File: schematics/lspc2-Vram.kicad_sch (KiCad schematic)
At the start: 2 parts

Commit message: update readme
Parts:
- renumbered 4B to 4B1, 5B to 5B1
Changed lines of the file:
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@@
     (effects (font (size 1.27 1.27)) (justify left bottom))
   )
-  (label "F15" (at 86.36 132.08 0)
-    (effects (font (size 1.27 1.27)) (justify left bottom))
-  )
-  (label "F14" (at 86.36 129.54 0)
-    (effects (font (size 1.27 1.27)) (justify left bottom))
-  )
-  (label "F12" (at 86.36 124.46 0)
-    (effects (font (size 1.27 1.27)) (justify left bottom))
-  )
-  (label "B13" (at 43.18 99.06 0)
+  (label "F15" (at 86.36 132.08 0) (fields_autoplaced)
+    (effects (font (size 1.27 1.27)) (justify left bottom))
+  )
+  (label "F14" (at 86.36 129.54 0) (fields_autoplaced)
+    (effects (font (size 1.27 1.27)) (justify left bottom))
+  )
+  (label "F12" (at 86.36 124.46 0) (fields_autoplaced)
+    (effects (font (size 1.27 1.27)) (justify left bottom))
+  )
+  (label "B13" (at 43.18 99.06 0) (fields_autoplaced)
     (effects (font (size 1.27 1.27)) (justify left bottom))
   )
@@
     (effects (font (size 1.27 1.27)) (justify left bottom))
   )
-  (label "F0" (at 86.36 66.04 0)
+  (label "F0" (at 86.36 66.04 0) (fields_autoplaced)
     (effects (font (size 1.27 1.27)) (justify left bottom))
   )
@@
     (effects (font (size 1.27 1.27)) (justify left bottom))
   )
-  (label "F13" (at 86.36 127 0)
-    (effects (font (size 1.27 1.27)) (justify left bottom))
-  )
-  (label "F6" (at 86.36 81.28 0)
-    (effects (font (size 1.27 1.27)) (justify left bottom))
-  )
-  (label "B12" (at 43.18 96.52 0)
-    (effects (font (size 1.27 1.27)) (justify left bottom))
-  )
-  (label "B11" (at 43.18 93.98 0)
-    (effects (font (size 1.27 1.27)) (justify left bottom))
-  )
-  (label "F4" (at 86.36 76.2 0)
-    (effects (font (size 1.27 1.27)) (justify left bottom))
-  )
-  (label "F11" (at 86.36 121.92 0)
-    (effects (font (size 1.27 1.27)) (justify left bottom))
-  )
-  (label "B0" (at 43.18 66.04 0)
+  (label "F13" (at 86.36 127 0) (fields_autoplaced)
+    (effects (font (size 1.27 1.27)) (justify left bottom))
+  )
+  (label "F6" (at 86.36 81.28 0) (fields_autoplaced)
+    (effects (font (size 1.27 1.27)) (justify left bottom))
+  )
+  (label "B12" (at 43.18 96.52 0) (fields_autoplaced)
+    (effects (font (size 1.27 1.27)) (justify left bottom))
+  )
+  (label "B11" (at 43.18 93.98 0) (fields_autoplaced)
+    (effects (font (size 1.27 1.27)) (justify left bottom))
+  )
+  (label "F4" (at 86.36 76.2 0) (fields_autoplaced)
+    (effects (font (size 1.27 1.27)) (justify left bottom))
+  )
+  (label "F11" (at 86.36 121.92 0) (fields_autoplaced)
+    (effects (font (size 1.27 1.27)) (justify left bottom))
+  )
+  (label "B0" (at 43.18 66.04 0) (fields_autoplaced)
     (effects (font (size 1.27 1.27)) (justify left bottom))
   )
@@
     (effects (font (size 1.27 1.27)) (justify left bottom))
   )
-  (label "B3" (at 43.18 73.66 0)
+  (label "B3" (at 43.18 73.66 0) (fields_autoplaced)
     (effects (font (size 1.27 1.27)) (justify left bottom))
   )
@@
     (effects (font (size 1.27 1.27)) (justify left bottom))
   )
-  (label "F8" (at 86.36 114.3 0)
-    (effects (font (size 1.27 1.27)) (justify left bottom))
-  )
-  (label "F1" (at 86.36 68.58 0)
-    (effects (font (size 1.27 1.27)) (justify left bottom))
-  )
-  (label "B10" (at 43.18 91.44 0)
-    (effects (font (size 1.27 1.27)) (justify left bottom))
-  )
-  (label "B4" (at 43.18 76.2 0)
+  (label "F8" (at 86.36 114.3 0) (fields_autoplaced)
+    (effects (font (size 1.27 1.27)) (justify left bottom))
+  )
+  (label "F1" (at 86.36 68.58 0) (fields_autoplaced)
+    (effects (font (size 1.27 1.27)) (justify left bottom))
+  )
+  (label "B10" (at 43.18 91.44 0) (fields_autoplaced)
+    (effects (font (size 1.27 1.27)) (justify left bottom))
+  )
+  (label "B4" (at 43.18 76.2 0) (fields_autoplaced)
     (effects (font (size 1.27 1.27)) (justify left bottom))
   )
@@
     (effects (font (size 1.27 1.27)) (justify left bottom))
   )
-  (label "B7" (at 43.18 83.82 0)
-    (effects (font (size 1.27 1.27)) (justify left bottom))
-  )
-  (label "B5" (at 43.18 78.74 0)
-    (effects (font (size 1.27 1.27)) (justify left bottom))
-  )
-  (label "B8" (at 43.18 86.36 0)
-    (effects (font (size 1.27 1.27)) (justify left bottom))
-  )
-  (label "F2" (at 86.36 71.12 0)
-    (effects (font (size 1.27 1.27)) (justify left bottom))
-  )
-  (label "B2" (at 43.18 71.12 0)
-    (effects (font (size 1.27 1.27)) (justify left bottom))
-  )
-  (label "F10" (at 86.36 119.38 0)
-    (effects (font (size 1.27 1.27)) (justify left bottom))
-  )
-  (label "F7" (at 86.36 83.82 0)
+  (label "B7" (at 43.18 83.82 0) (fields_autoplaced)
+    (effects (font (size 1.27 1.27)) (justify left bottom))
+  )
+  (label "B5" (at 43.18 78.74 0) (fields_autoplaced)
+    (effects (font (size 1.27 1.27)) (justify left bottom))
+  )
+  (label "B8" (at 43.18 86.36 0) (fields_autoplaced)
+    (effects (font (size 1.27 1.27)) (justify left bottom))
+  )
+  (label "F2" (at 86.36 71.12 0) (fields_autoplaced)
+    (effects (font (size 1.27 1.27)) (justify left bottom))
+  )
+  (label "B2" (at 43.18 71.12 0) (fields_autoplaced)
+    (effects (font (size 1.27 1.27)) (justify left bottom))
+  )
+  (label "F10" (at 86.36 119.38 0) (fields_autoplaced)
+    (effects (font (size 1.27 1.27)) (justify left bottom))
+  )
+  (label "F7" (at 86.36 83.82 0) (fields_autoplaced)
     (effects (font (size 1.27 1.27)) (justify left bottom))
   )
@@
     (effects (font (size 1.27 1.27)) (justify left bottom))
   )
-  (label "F9" (at 86.36 116.84 0)
-    (effects (font (size 1.27 1.27)) (justify left bottom))
-  )
-  (label "B9" (at 43.18 88.9 0)
+  (label "F9" (at 86.36 116.84 0) (fields_autoplaced)
+    (effects (font (size 1.27 1.27)) (justify left bottom))
+  )
+  (label "B9" (at 43.18 88.9 0) (fields_autoplaced)
     (effects (font (size 1.27 1.27)) (justify left bottom))
   )
@@
     (effects (font (size 1.27 1.27)) (justify left bottom))
   )
-  (label "F5" (at 86.36 78.74 0)
+  (label "F5" (at 86.36 78.74 0) (fields_autoplaced)
     (effects (font (size 1.27 1.27)) (justify left bottom))
   )
@@
     (effects (font (size 1.27 1.27)) (justify left bottom))
   )
-  (label "F3" (at 86.36 73.66 0)
+  (label "F3" (at 86.36 73.66 0) (fields_autoplaced)
     (effects (font (size 1.27 1.27)) (justify left bottom))
   )
@@
     (effects (font (size 1.27 1.27)) (justify left bottom))
   )
-  (label "B1" (at 43.18 68.58 0)
-    (effects (font (size 1.27 1.27)) (justify left bottom))
-  )
-  (label "B14" (at 43.18 101.6 0)
-    (effects (font (size 1.27 1.27)) (justify left bottom))
-  )
-  (label "B6" (at 43.18 81.28 0)
+  (label "B1" (at 43.18 68.58 0) (fields_autoplaced)
+    (effects (font (size 1.27 1.27)) (justify left bottom))
+  )
+  (label "B14" (at 43.18 101.6 0) (fields_autoplaced)
+    (effects (font (size 1.27 1.27)) (justify left bottom))
+  )
+  (label "B6" (at 43.18 81.28 0) (fields_autoplaced)
     (effects (font (size 1.27 1.27)) (justify left bottom))
   )
@@
   (symbol (lib_id "Memory_RAM:KM62256CLP") (at 64.77 83.82 0) (unit 1)
     (in_bom yes) (on_board yes) (dnp no)
-    (property "Reference" "4B" (at 54.61 62.23 0)
+    (property "Reference" "4B1" (at 54.61 62.23 0)
       (effects (font (size 1.27 1.27)) (justify left))
     )
@@
       (project "MVS"
         (path "/8d0803ab-15ed-47a7-8dcb-ab27dc5b29c2/5f943e9e-0280-4d4f-b6a1-cb23eca420c0"
-          (reference "4B") (unit 1)
+          (reference "4B1") (unit 1)
         )
       )
@@
   (symbol (lib_id "Memory_RAM:KM62256CLP") (at 64.77 132.08 0) (unit 1)
     (in_bom yes) (on_board yes) (dnp no)
-    (property "Reference" "5B" (at 54.61 110.49 0)
+    (property "Reference" "5B1" (at 54.61 110.49 0)
       (effects (font (size 1.27 1.27)) (justify left))
     )
@@
       (project "MVS"
         (path "/8d0803ab-15ed-47a7-8dcb-ab27dc5b29c2/5f943e9e-0280-4d4f-b6a1-cb23eca420c0"
-          (reference "5B") (unit 1)
+          (reference "5B1") (unit 1)
         )
       )

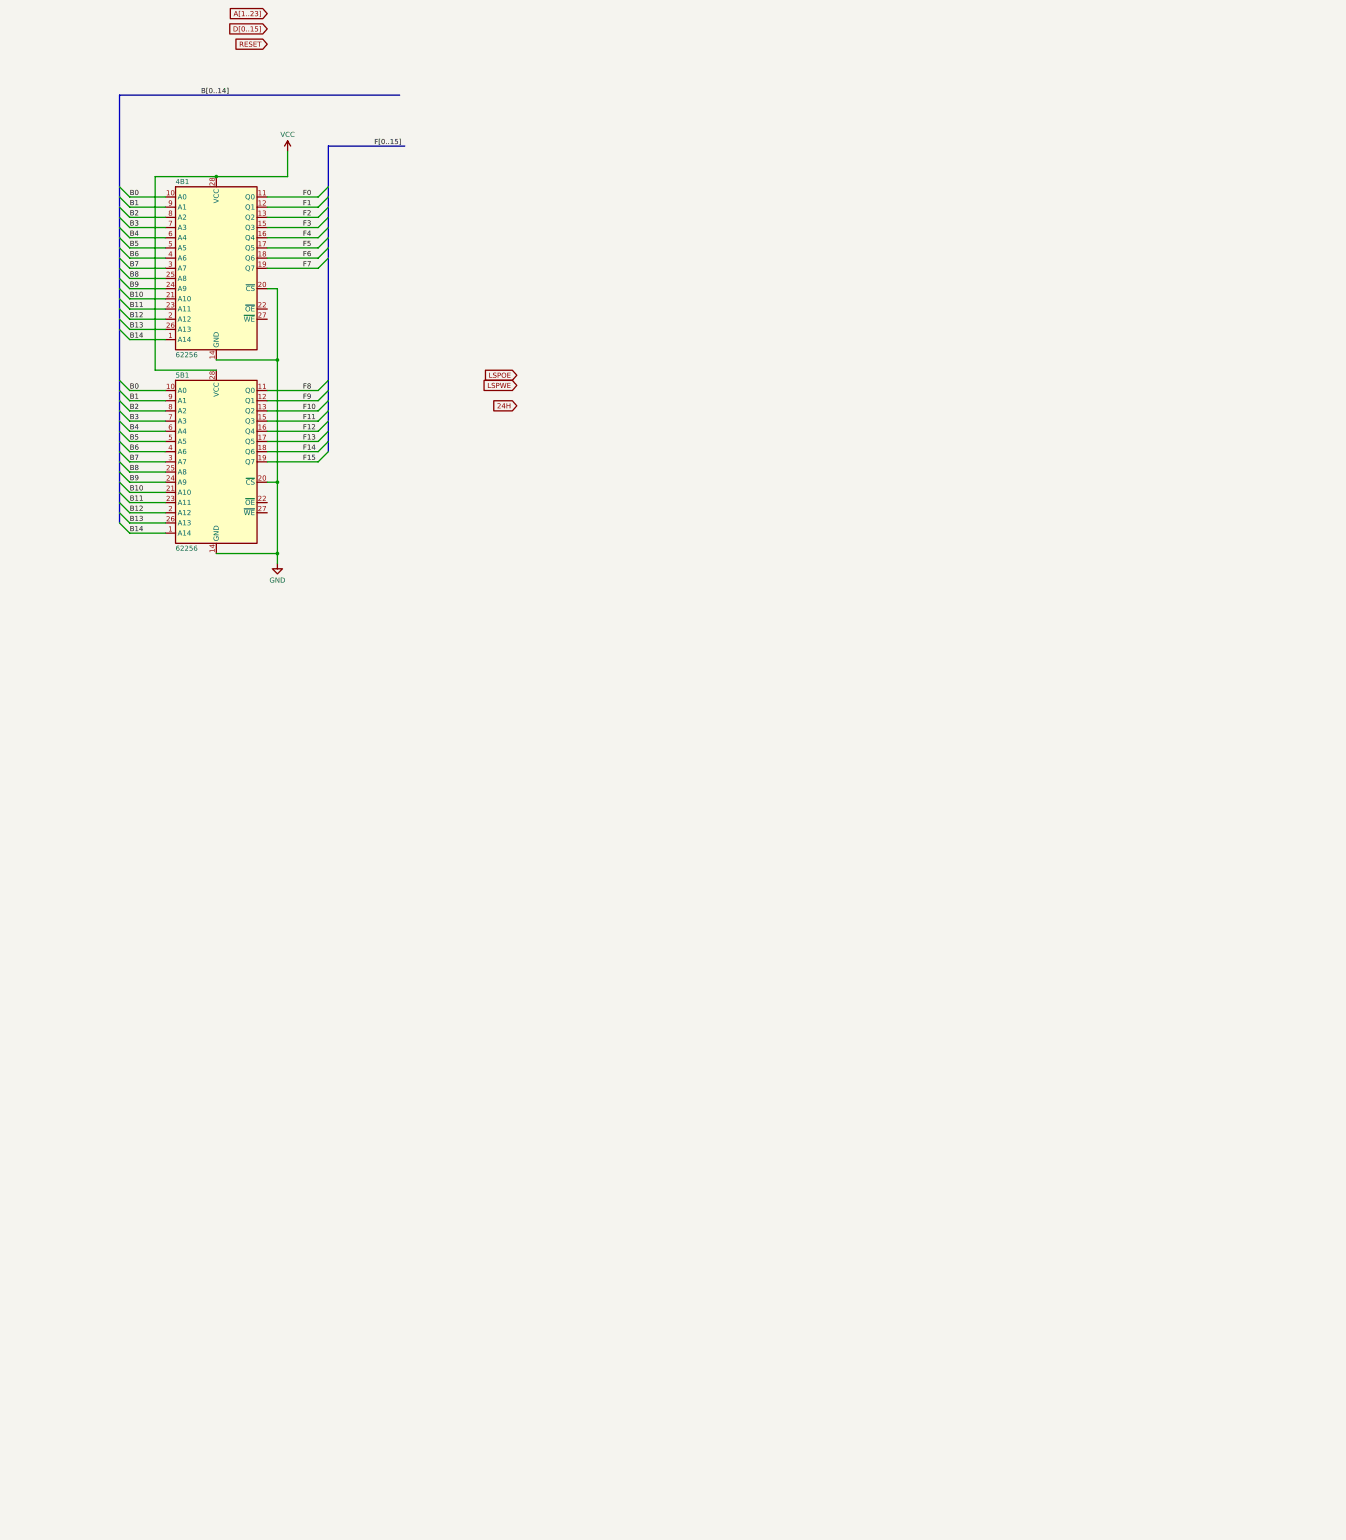
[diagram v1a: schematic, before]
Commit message: update "main" schematics
Adding LSPC2-A2, NEO-B1, L0 ROM
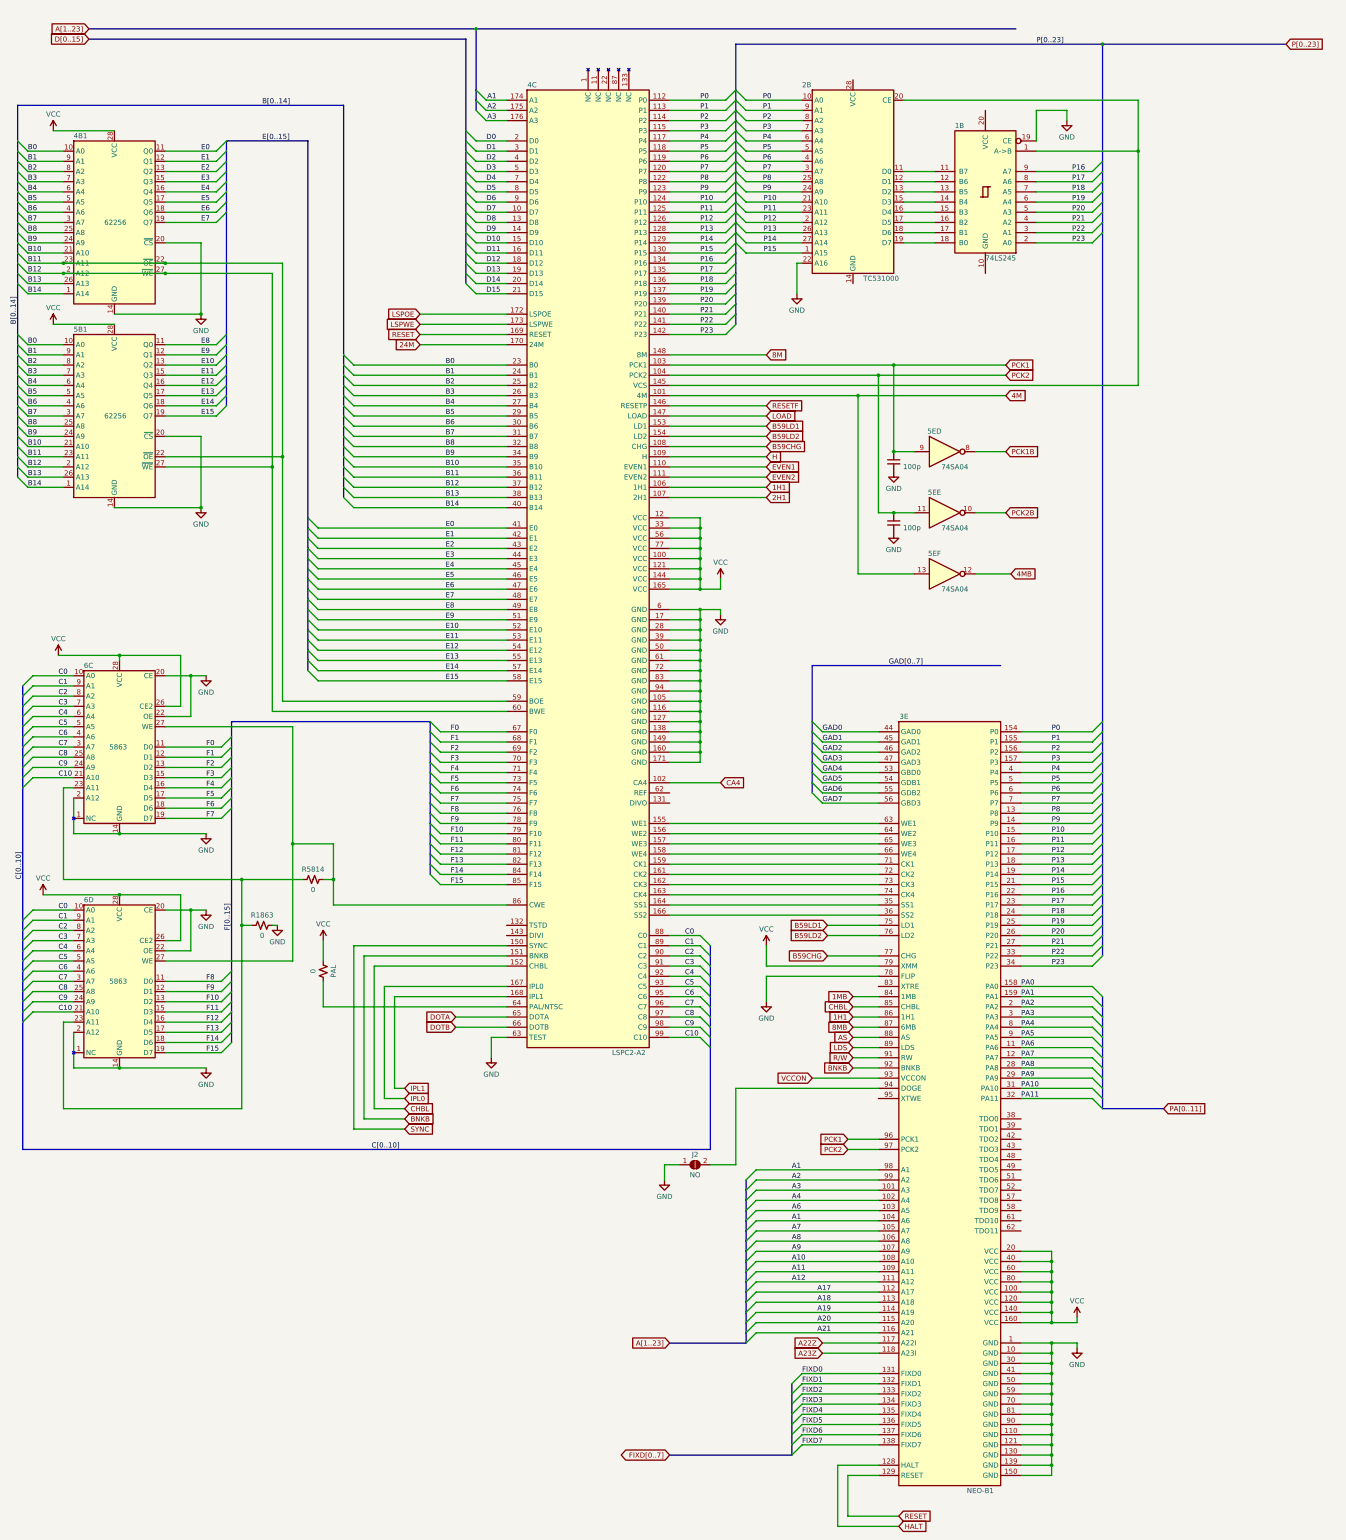
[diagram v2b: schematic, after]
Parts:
- added 1B: 74LS245, symbol 74xx:74LS245
- added 2B: TC531000, Package_DIP:DIP-28_W15.24mm, symbol 0-Custom-SNK:TC531000AP
- added 3E: NEO-B1, symbol 0-Custom-SNK:NEO-B1
- added 4C: LSPC2-A2, symbol 0-Custom-SNK:LSPC2-A2
- added 5E: 74SA04, symbol 74xx:74HC04
- added 6C, 6D: 5863, Package_DIP:DIP-28_W7.62mm, symbol 0-Custom-SNK:CXK5863AP
- added C4, C5: 100p, symbol Device:C_Small
- added J2: NO, symbol Jumper:SolderJumper_2_Open
- added PAL, R1863, R5814: 0, symbol Device:R_Small_US
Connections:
- net B0: now also 4C.23 (B0)
- net B1: now also 4C.24 (B1)
- net B10: now also 4C.35 (B10)
- net B11: now also 4B1.22 (~{OE}), 5B1.22 (~{OE}), 4C.36 (B11), 4C.59 (BOE)
- net B12: now also 4B1.27 (~{WE}), 5B1.27 (~{WE}), 4C.37 (B12), 4C.60 (BWE)
- net B13: now also 4C.38 (B13)
- net B14: now also 4C.40 (B14)
- net B2: now also 4C.25 (B2)
- net B3: now also 4C.26 (B3)
- net B4: now also 4C.27 (B4)
- net B5: now also 4C.29 (B5)
- net B6: now also 4C.30 (B6)
- net B7: now also 4C.31 (B7)
- net B8: now also 4C.32 (B8)
- net B9: now also 4C.34 (B9)
- net F0: now also 4C.67 (F0), 6C.11 (D0); no longer 4B1.11 (Q0)
- net F1: now also 4C.68 (F1), 6C.12 (D1); no longer 4B1.12 (Q1)
- net F10: now also 4C.79 (F10), 6D.13 (D2); no longer 5B1.13 (Q2)
- net F11: now also 4C.80 (F11), 6D.15 (D3); no longer 5B1.15 (Q3)
- net F12: now also 4C.81 (F12), 6D.16 (D4); no longer 5B1.16 (Q4)
- net F13: now also 4C.82 (F13), 6D.17 (D5); no longer 5B1.17 (Q5)
- net F14: now also 4C.84 (F14), 6D.18 (D6); no longer 5B1.18 (Q6)
- net F15: now also 4C.85 (F15), 6D.19 (D7); no longer 5B1.19 (Q7)
- net F2: now also 4C.69 (F2), 6C.13 (D2); no longer 4B1.13 (Q2)
- net F3: now also 4C.70 (F3), 6C.15 (D3); no longer 4B1.15 (Q3)
- net F4: now also 4C.71 (F4), 6C.16 (D4); no longer 4B1.16 (Q4)
- net F5: now also 4C.73 (F5), 6C.17 (D5); no longer 4B1.17 (Q5)
- net F6: now also 4C.74 (F6), 6C.18 (D6); no longer 4B1.18 (Q6)
- net F7: now also 4C.75 (F7), 6C.19 (D7); no longer 4B1.19 (Q7)
- net F8: now also 4C.76 (F8), 6D.11 (D0); no longer 5B1.11 (Q0)
- net F9: now also 4C.78 (F9), 6D.12 (D1); no longer 5B1.12 (Q1)
- net GND: now also 1B.19 (CE), 2B.22 (A16), 3E.1 (GND), 3E.10 (GND), 3E.110 (GND), 3E.121 (GND), 3E.130 (GND), 3E.139 (GND), 3E.150 (GND), 3E.30 (GND), 3E.41 (GND), 3E.50 (GND), 3E.59 (GND), 3E.70 (GND), 3E.78 (FLIP), 3E.81 (GND), 3E.90 (GND), 4C.105 (GND), 4C.116 (GND), 4C.127 (GND), 4C.138 (GND), 4C.149 (GND), 4C.160 (GND), 4C.17 (GND), 4C.171 (GND), 4C.28 (GND), 4C.39 (GND), 4C.50 (GND), 4C.6 (GND), 4C.61 (GND), 4C.63 (TEST), 4C.72 (GND), 4C.83 (GND), 4C.94 (GND), 6C.14 (GND), 6C.2 (A12), 6C.20 (CE), 6C.22 (OE), 6D.14 (GND), 6D.2 (A12), 6D.20 (CE), 6D.22 (OE), C4.2, C5.2, J2.1 (A), R1863.2
- net LSPOE: now also 4C.172 (LSPOE)
- net LSPWE: now also 4C.173 (LSPWE)
- net RESET: now also 3E.129 (RESET), 4C.169 (RESET)
- net VCC: now also 3E.100 (VCC), 3E.120 (VCC), 3E.140 (VCC), 3E.160 (VCC), 3E.20 (VCC), 3E.40 (VCC), 3E.60 (VCC), 3E.79 (XMM), 3E.80 (VCC), 4C.100 (VCC), 4C.12 (VCC), 4C.121 (VCC), 4C.144 (VCC), 4C.165 (VCC), 4C.33 (VCC), 4C.56 (VCC), 4C.77 (VCC), 6C.26 (CE2), 6C.28 (VCC), 6D.26 (CE2), 6D.28 (VCC), PAL.1
- new net: 6C.23 (A11), 6D.23 (A11), R1863.1, R5814.1
- new net: 4C.86 (CWE), 6C.27 (WE), 6D.27 (WE), R5814.2
- new net: 1B.11 (B7), 2B.11 (D0)
- new net: 1B.12 (B6), 2B.12 (D1)
- new net: 1B.13 (B5), 2B.13 (D2)
- new net: 1B.14 (B4), 2B.15 (D3)
- new net: 1B.15 (B3), 2B.16 (D4)
- new net: 1B.16 (B2), 2B.17 (D5)
- new net: 1B.17 (B1), 2B.18 (D6)
- new net: 1B.18 (B0), 2B.19 (D7)
- new net: 1B.1 (A->B), 2B.20 (CE), 4C.145 (VCS)
- new net: 3E.94 (DOGE), J2.2 (B)
- new net: 4C.64 (PAL/NTSC), PAL.2
- new net: 3E.63 (WE1), 4C.155 (WE1)
- new net: 3E.64 (WE2), 4C.156 (WE2)
- new net: 3E.65 (WE3), 4C.157 (WE3)
- new net: 3E.66 (WE4), 4C.158 (WE4)
- new net: 3E.71 (CK1), 4C.159 (CK1)
- new net: 3E.72 (CK2), 4C.161 (CK2)
- new net: 3E.73 (CK3), 4C.162 (CK3)
- new net: 3E.74 (CK4), 4C.163 (CK4)
- new net: 3E.35 (SS1), 4C.164 (SS1)
- new net: 3E.36 (SS2), 4C.166 (SS2)
- new net: 3E.119 (NC), 3E.122 (NC), 3E.123 (NC), 3E.124 (NC), 3E.125 (NC), 3E.126 (NC), 3E.127 (NC), 3E.141 (NC), 3E.142 (NC), 3E.143 (NC), 3E.144 (NC), 3E.145 (NC), 3E.146 (NC), 3E.147 (NC), 3E.148 (NC), 3E.149 (NC), 3E.151 (NC), 3E.152 (NC), 3E.153 (NC), 3E.37 (NC), 3E.67 (NC), 3E.68 (NC), 3E.69 (NC), 3E.82 (NC)
- new net 1H1: 3E.86 (1H1), 4C.106 (1H1)
- new net 1MB: 3E.84 (1MB)
- new net 24M: 4C.170 (24M)
- new net 2H1: 4C.107 (2H1)
- new net 4M: 4C.101 (4M), 5E.13
- new net 4MB: 5E.12
- new net 8M: 4C.148 (8M)
- new net 8MB: 3E.87 (6MB)
- new net A1: 3E.104 (A6), 3E.98 (A1), 4C.174 (A1)
- new net A10: 3E.108 (A10)
- new net A11: 3E.109 (A11)
- new net A12: 3E.111 (A12)
- new net A17: 3E.112 (A17)
- new net A18: 3E.113 (A18)
- new net A19: 3E.114 (A19)
- new net A2: 3E.99 (A2), 4C.175 (A2)
- new net A20: 3E.115 (A20)
- new net A21: 3E.116 (A21)
- new net A22Z: 3E.117 (A22I)
- new net A23Z: 3E.118 (A23I)
- new net A3: 3E.101 (A3), 4C.176 (A3)
- new net A4: 3E.102 (A4)
- new net A6: 3E.103 (A5)
- new net A7: 3E.105 (A7)
- new net A8: 3E.106 (A8)
- new net A9: 3E.107 (A9)
- new net AS: 3E.88 (AS)
- new net B59CHG: 3E.77 (CHG), 4C.108 (CHG)
- new net B59LD1: 3E.75 (LD1), 4C.153 (LD1)
- new net B59LD2: 3E.76 (LD2), 4C.154 (LD2)
- new net BNKB: 3E.92 (BNKB), 4C.151 (BNKB)
- new net C0: 4C.88 (C0), 6C.10 (A0), 6D.10 (A0)
- new net C1: 4C.89 (C1), 6C.9 (A1), 6D.9 (A1)
- new net C10: 4C.99 (C10), 6C.21 (A10), 6D.21 (A10)
- new net C2: 4C.90 (C2), 6C.8 (A2), 6D.8 (A2)
- new net C3: 4C.91 (C3), 6C.7 (A3), 6D.7 (A3)
- new net C4: 4C.92 (C4), 6C.6 (A4), 6D.6 (A4)
- new net C5: 4C.93 (C5), 6C.5 (A5), 6D.5 (A5)
- new net C6: 4C.95 (C6), 6C.4 (A6), 6D.4 (A6)
- new net C7: 4C.96 (C7), 6C.3 (A7), 6D.3 (A7)
- new net C8: 4C.97 (C8), 6C.25 (A8), 6D.25 (A8)
- new net C9: 4C.98 (C9), 6C.24 (A9), 6D.24 (A9)
- new net CA4: 4C.102 (CA4)
- new net CHBL: 3E.85 (CHBL), 4C.152 (CHBL)
- new net D0: 4C.2 (D0)
- new net D1: 4C.3 (D1)
- new net D10: 4C.15 (D10)
- new net D11: 4C.16 (D11)
- new net D12: 4C.18 (D12)
- new net D13: 4C.19 (D13)
- new net D14: 4C.20 (D14)
- new net D15: 4C.21 (D15)
- new net D2: 4C.4 (D2)
- new net D3: 4C.5 (D3)
- new net D4: 4C.7 (D4)
- new net D5: 4C.8 (D5)
- new net D6: 4C.9 (D6)
- new net D7: 4C.10 (D7)
- new net D8: 4C.13 (D8)
- new net D9: 4C.14 (D9)
- new net DOTA: 4C.65 (DOTA)
- new net DOTB: 4C.66 (DOTB)
- new net E0: 4B1.11 (Q0), 4C.41 (E0)
- new net E1: 4B1.12 (Q1), 4C.42 (E1)
- new net E10: 4C.52 (E10), 5B1.13 (Q2)
- new net E11: 4C.53 (E11), 5B1.15 (Q3)
- new net E12: 4C.54 (E12), 5B1.16 (Q4)
- new net E13: 4C.55 (E13), 5B1.17 (Q5)
- new net E14: 4C.57 (E14), 5B1.18 (Q6)
- new net E15: 4C.58 (E15), 5B1.19 (Q7)
- new net E2: 4B1.13 (Q2), 4C.43 (E2)
- new net E3: 4B1.15 (Q3), 4C.44 (E3)
- new net E4: 4B1.16 (Q4), 4C.45 (E4)
- new net E5: 4B1.17 (Q5), 4C.46 (E5)
- new net E6: 4B1.18 (Q6), 4C.47 (E6)
- new net E7: 4B1.19 (Q7), 4C.48 (E7)
- new net E8: 4C.49 (E8), 5B1.11 (Q0)
- new net E9: 4C.51 (E9), 5B1.12 (Q1)
- new net EVEN1: 4C.110 (EVEN1)
- new net EVEN2: 4C.111 (EVEN2)
- new net FIXD0: 3E.131 (FIXD0)
- new net FIXD1: 3E.132 (FIXD1)
- new net FIXD2: 3E.133 (FIXD2)
- new net FIXD3: 3E.134 (FIXD3)
- new net FIXD4: 3E.135 (FIXD4)
- new net FIXD5: 3E.136 (FIXD5)
- new net FIXD6: 3E.137 (FIXD6)
- new net FIXD7: 3E.138 (FIXD7)
- new net GAD0: 3E.44 (GAD0)
- new net GAD1: 3E.45 (GAD1)
- new net GAD2: 3E.46 (GAD2)
- new net GAD3: 3E.47 (GAD3)
- new net GAD4: 3E.53 (GBD0)
- new net GAD5: 3E.54 (GDB1)
- new net GAD6: 3E.55 (GDB2)
- new net GAD7: 3E.56 (GBD3)
- new net H: 4C.109 (H)
- new net HALT: 3E.128 (HALT)
- new net IPL0: 4C.167 (IPL0)
- new net IPL1: 4C.168 (IPL1)
- new net LDS: 3E.89 (LDS)
- new net LOAD: 4C.147 (LOAD)
- new net P0: 2B.10 (A0), 3E.154 (P0), 4C.112 (P0)
- new net P1: 2B.9 (A1), 3E.155 (P1), 4C.113 (P1)
- new net P10: 2B.21 (A10), 3E.15 (P10), 4C.124 (P10)
- new net P11: 2B.23 (A11), 3E.16 (P11), 4C.125 (P11)
- new net P12: 2B.2 (A12), 3E.17 (P12), 4C.126 (P12)
- new net P13: 2B.26 (A13), 3E.18 (P13), 4C.128 (P13)
- new net P14: 2B.27 (A14), 3E.19 (P14), 4C.129 (P14)
- new net P15: 2B.1 (A15), 3E.21 (P15), 4C.130 (P15)
- new net P16: 1B.9 (A7), 3E.22 (P16), 4C.134 (P16)
- new net P17: 1B.8 (A6), 3E.23 (P17), 4C.135 (P17)
- new net P18: 1B.7 (A5), 3E.24 (P18), 4C.136 (P18)
- new net P19: 1B.6 (A4), 3E.25 (P19), 4C.137 (P19)
- new net P2: 2B.8 (A2), 3E.156 (P2), 4C.114 (P2)
- new net P20: 1B.5 (A3), 3E.26 (P20), 4C.139 (P20)
- new net P21: 1B.4 (A2), 3E.27 (P21), 4C.140 (P21)
- new net P22: 1B.3 (A1), 3E.33 (P22), 4C.141 (P22)
- new net P23: 1B.2 (A0), 3E.34 (P23), 4C.142 (P23)
- new net P3: 2B.7 (A3), 3E.157 (P3), 4C.115 (P3)
- new net P4: 2B.6 (A4), 3E.4 (P4), 4C.117 (P4)
- new net P5: 2B.5 (A5), 3E.5 (P5), 4C.118 (P5)
- new net P6: 2B.4 (A6), 3E.6 (P6), 4C.119 (P6)
- new net P7: 2B.3 (A7), 3E.7 (P7), 4C.120 (P7)
- new net P8: 2B.25 (A8), 3E.13 (P8), 4C.122 (P8)
- new net P9: 2B.24 (A9), 3E.14 (P9), 4C.123 (P9)
- new net PA0: 3E.158 (PA0)
- new net PA1: 3E.159 (PA1)
- new net PA10: 3E.31 (PA10)
- new net PA11: 3E.32 (PA11)
- new net PA2: 3E.2 (PA2)
- new net PA3: 3E.3 (PA3)
- new net PA4: 3E.8 (PA4)
- new net PA5: 3E.9 (PA5)
- new net PA6: 3E.11 (PA6)
- new net PA7: 3E.12 (PA7)
- new net PA8: 3E.28 (PA8)
- new net PA9: 3E.29 (PA9)
- new net PCK1: 3E.96 (PCK1), 4C.103 (PCK1), 5E.9, C4.1
- new net PCK1B: 5E.8
- new net PCK2: 3E.97 (PCK2), 4C.104 (PCK2), 5E.11, C5.1
- new net PCK2B: 5E.10
- new net RESETF: 4C.146 (RESETP)
- new net R/W: 3E.91 (RW)
- new net SYNC: 4C.150 (SYNC)
- new net VCCON: 3E.93 (VCCON)
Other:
- moved on the sheet: 4B1, 5B1
